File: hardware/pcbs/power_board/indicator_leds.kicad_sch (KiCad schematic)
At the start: 10 parts, among them Q4 BSS138, Q5 BSS138, Q6 BSS138

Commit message: audio_board, power_board: update shop and part links
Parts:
- R35, R36, R37: Part (none) -> R 10Ω 125mW 5% 0805
- R38, R39, R40: Part (none) -> R 1.8kΩ 125mW 5% 0805
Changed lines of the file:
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@@
+			)
+		)
+		(property "Part" "R 10Ω 125mW 5% 0805"
+			(at 123.19 96.52 0)
+			(effects
+				(font
+					(size 1.27 1.27)
+				)
+				(hide yes)
 			)
 		)
@@
 		)
 		(property "LCSC" "C17415"
+			(at 123.19 132.08 0)
+			(effects
+				(font
+					(size 1.27 1.27)
+				)
+				(hide yes)
+			)
+		)
+		(property "Part" "R 10Ω 125mW 5% 0805"
 			(at 123.19 132.08 0)
 			(effects
@@
 			)
 		)
+		(property "Part" "R 1.8kΩ 125mW 5% 0805"
+			(at 153.67 64.77 0)
+			(effects
+				(font
+					(size 1.27 1.27)
+				)
+				(hide yes)
+			)
+		)
 		(pin "2"
 		)
@@
 			)
 		)
+		(property "Part" "R 1.8kΩ 125mW 5% 0805"
+			(at 148.59 64.77 0)
+			(effects
+				(font
+					(size 1.27 1.27)
+				)
+				(hide yes)
+			)
+		)
 		(pin "2"
 		)
@@
 			)
 		)
+		(property "Part" "R 10Ω 125mW 5% 0805"
+			(at 123.19 114.3 0)
+			(effects
+				(font
+					(size 1.27 1.27)
+				)
+				(hide yes)
+			)
+		)
 		(pin "1"
 		)
@@
 			(at 143.51 64.77 0)
 			(effects
+				(font
+					(size 1.27 1.27)
+				)
+				(hide yes)
+			)
+		)
+		(property "Part" "R 1.8kΩ 125mW 5% 0805"
+			(at 143.51 64.77 0)
+			(effects

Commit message: power_board: BIGGER inductors
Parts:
- R35, R36, R37: value 10Ω -> 10Ω
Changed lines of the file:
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@@
 			)
 		)
-		(property "Value" "10Ω "
+		(property "Value" "10Ω"
 			(at 123.19 99.06 90)
 			(effects
@@
 			)
 		)
-		(property "Value" "10Ω "
+		(property "Value" "10Ω"
 			(at 123.19 134.62 90)
 			(effects
@@
 			)
 		)
-		(property "Value" "10Ω "
+		(property "Value" "10Ω"
 			(at 123.19 116.84 90)
 			(effects

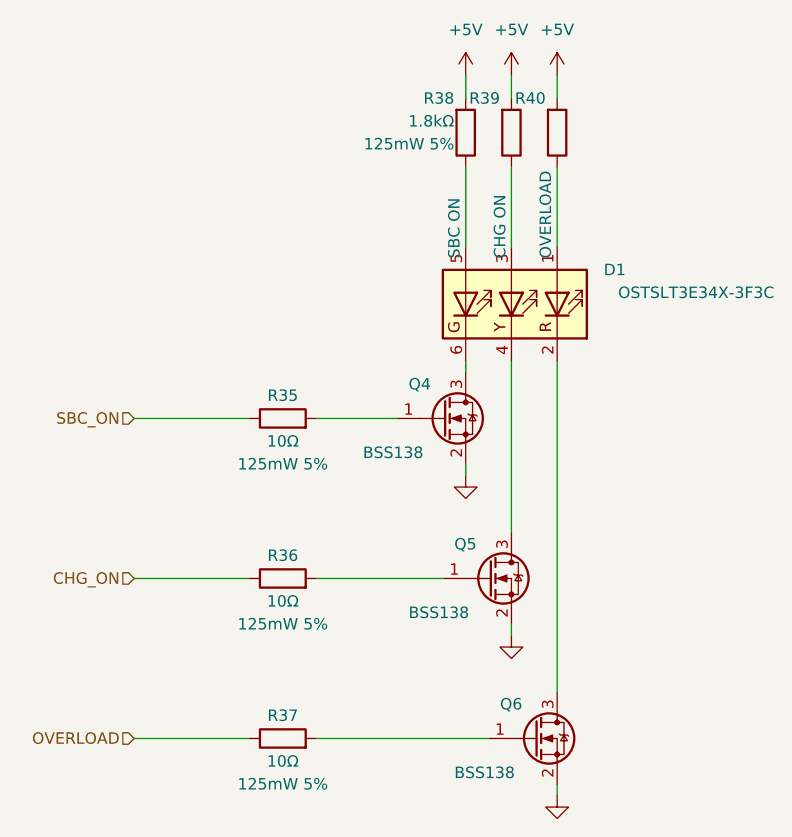
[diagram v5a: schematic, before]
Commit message: power_board: use USB3-A passthrough connector and fix chg EN
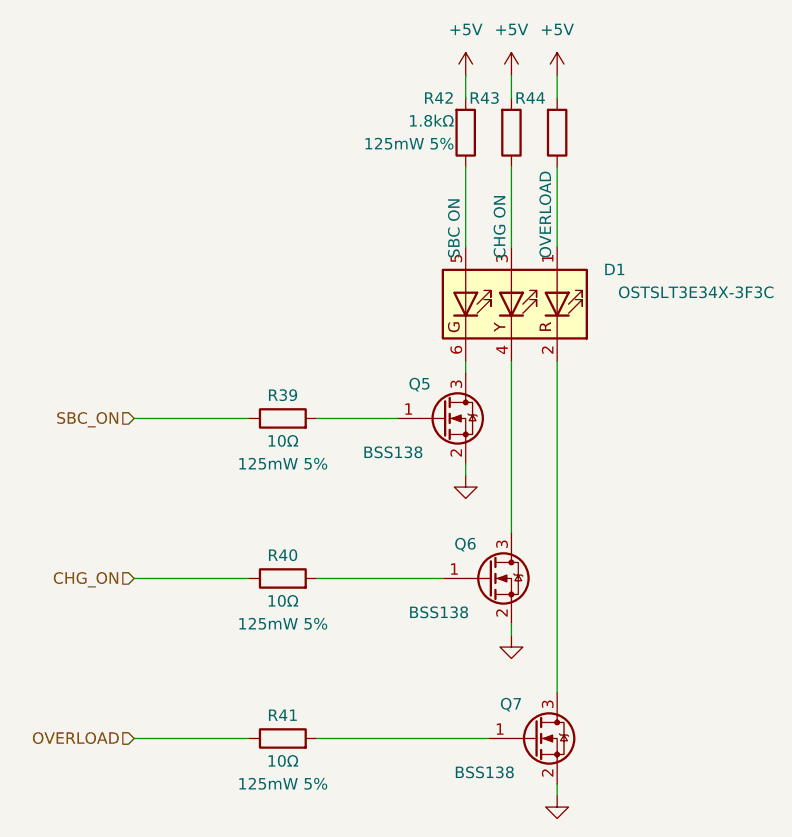
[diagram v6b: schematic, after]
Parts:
- renumbered Q4 to Q5, Q5 to Q6, Q6 to Q7, R35 to R39, R36 to R40, R37 to R41, R38 to R42, R39 to R43, R40 to R44
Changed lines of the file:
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@@
 		(on_board yes)
 		(dnp no)
-		(property "Reference" "Q6"
+		(property "Reference" "Q7"
 			(at 147.32 128.27 0)
 			(effects
@@
 			(project "power_board"
 				(path "/4b166175-80a4-48c6-994d-6e62a6160b87/9db409a6-3616-4139-9d4b-1b510fbe4a7d"
-					(reference "Q6")
+					(reference "Q7")
 					(unit 1)
 				)
@@
 		(on_board yes)
 		(dnp no)
-		(property "Reference" "R35"
+		(property "Reference" "R39"
 			(at 123.19 93.98 90)
 			(effects
@@
 			(project "power_board"
 				(path "/4b166175-80a4-48c6-994d-6e62a6160b87/9db409a6-3616-4139-9d4b-1b510fbe4a7d"
-					(reference "R35")
+					(reference "R39")
 					(unit 1)
 				)
@@
 		(on_board yes)
 		(dnp no)
-		(property "Reference" "R37"
+		(property "Reference" "R41"
 			(at 123.19 129.54 90)
 			(effects
@@
 			(project "power_board"
 				(path "/4b166175-80a4-48c6-994d-6e62a6160b87/9db409a6-3616-4139-9d4b-1b510fbe4a7d"
-					(reference "R37")
+					(reference "R41")
 					(unit 1)
 				)
@@
 		(on_board yes)
 		(dnp no)
-		(property "Reference" "R40"
+		(property "Reference" "R44"
 			(at 152.4 60.96 0)
 			(effects
@@
 			(project "power_board"
 				(path "/4b166175-80a4-48c6-994d-6e62a6160b87/9db409a6-3616-4139-9d4b-1b510fbe4a7d"
-					(reference "R40")
+					(reference "R44")
 					(unit 1)
 				)
@@
 		(on_board yes)
 		(dnp no)
-		(property "Reference" "R39"
+		(property "Reference" "R43"
 			(at 147.32 60.96 0)
 			(effects
@@
 			(project "power_board"
 				(path "/4b166175-80a4-48c6-994d-6e62a6160b87/9db409a6-3616-4139-9d4b-1b510fbe4a7d"
-					(reference "R39")
+					(reference "R43")
 					(unit 1)
 				)
@@
 		(on_board yes)
 		(dnp no)
-		(property "Reference" "R36"
+		(property "Reference" "R40"
 			(at 123.19 111.76 90)
 			(effects
@@
 			(project "power_board"
 				(path "/4b166175-80a4-48c6-994d-6e62a6160b87/9db409a6-3616-4139-9d4b-1b510fbe4a7d"
-					(reference "R36")
+					(reference "R40")
 					(unit 1)
 				)
@@
 		(on_board yes)
 		(dnp no)
-		(property "Reference" "Q4"
+		(property "Reference" "Q5"
 			(at 137.16 92.71 0)
 			(effects
@@
 			(project "power_board"
 				(path "/4b166175-80a4-48c6-994d-6e62a6160b87/9db409a6-3616-4139-9d4b-1b510fbe4a7d"
-					(reference "Q4")
+					(reference "Q5")
 					(unit 1)
 				)
@@
 		(on_board yes)
 		(dnp no)
-		(property "Reference" "R38"
+		(property "Reference" "R42"
 			(at 142.24 60.96 0)
 			(effects
@@
 			(project "power_board"
 				(path "/4b166175-80a4-48c6-994d-6e62a6160b87/9db409a6-3616-4139-9d4b-1b510fbe4a7d"
-					(reference "R38")
+					(reference "R42")
 					(unit 1)
 				)
@@
 		(on_board yes)
 		(dnp no)
-		(property "Reference" "Q5"
+		(property "Reference" "Q6"
 			(at 142.24 110.49 0)
 			(effects
@@
 			(project "power_board"
 				(path "/4b166175-80a4-48c6-994d-6e62a6160b87/9db409a6-3616-4139-9d4b-1b510fbe4a7d"
-					(reference "Q5")
-					(unit 1)
-				)
+					(reference "Q6")
+					(unit 1)
+				)

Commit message: power_board: add protection resistor to overload signal
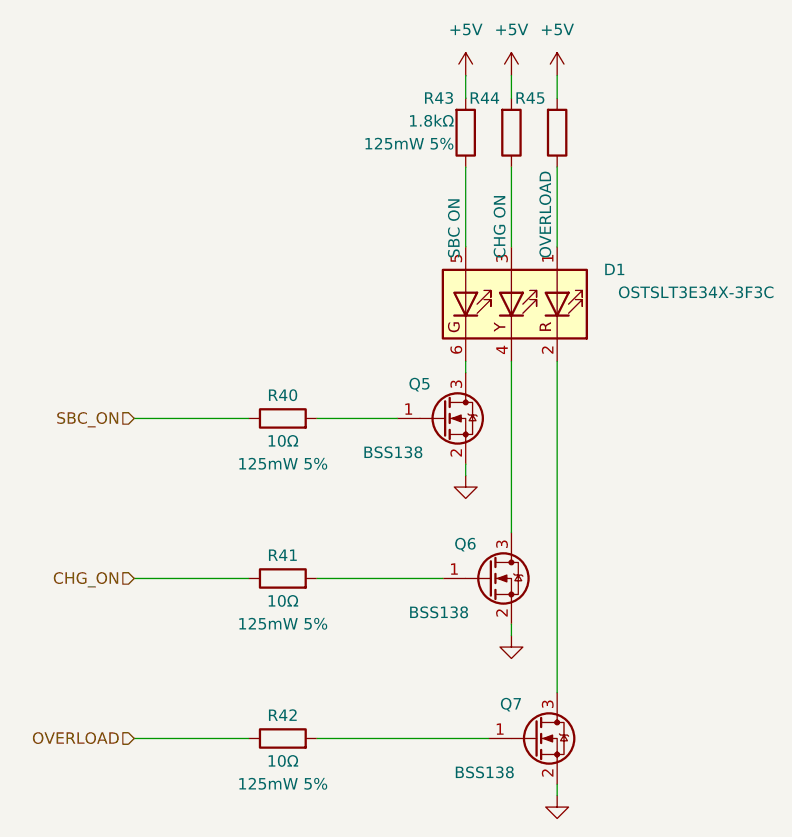
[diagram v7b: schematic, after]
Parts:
- renumbered R39 to R40, R40 to R41, R41 to R42, R42 to R43, R43 to R44, R44 to R45
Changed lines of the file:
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@@
 		(on_board yes)
 		(dnp no)
-		(property "Reference" "R39"
+		(property "Reference" "R40"
 			(at 123.19 93.98 90)
 			(effects
@@
 			(project "power_board"
 				(path "/4b166175-80a4-48c6-994d-6e62a6160b87/9db409a6-3616-4139-9d4b-1b510fbe4a7d"
-					(reference "R39")
+					(reference "R40")
 					(unit 1)
 				)
@@
 		(on_board yes)
 		(dnp no)
-		(property "Reference" "R41"
+		(property "Reference" "R42"
 			(at 123.19 129.54 90)
 			(effects
@@
 			(project "power_board"
 				(path "/4b166175-80a4-48c6-994d-6e62a6160b87/9db409a6-3616-4139-9d4b-1b510fbe4a7d"
-					(reference "R41")
+					(reference "R42")
 					(unit 1)
 				)
@@
 		(on_board yes)
 		(dnp no)
-		(property "Reference" "R44"
+		(property "Reference" "R45"
 			(at 152.4 60.96 0)
 			(effects
@@
 			(project "power_board"
 				(path "/4b166175-80a4-48c6-994d-6e62a6160b87/9db409a6-3616-4139-9d4b-1b510fbe4a7d"
-					(reference "R44")
+					(reference "R45")
 					(unit 1)
 				)
@@
 		(on_board yes)
 		(dnp no)
-		(property "Reference" "R43"
+		(property "Reference" "R44"
 			(at 147.32 60.96 0)
 			(effects
@@
 			(project "power_board"
 				(path "/4b166175-80a4-48c6-994d-6e62a6160b87/9db409a6-3616-4139-9d4b-1b510fbe4a7d"
-					(reference "R43")
+					(reference "R44")
 					(unit 1)
 				)
@@
 		(on_board yes)
 		(dnp no)
-		(property "Reference" "R40"
+		(property "Reference" "R41"
 			(at 123.19 111.76 90)
 			(effects
@@
 			(project "power_board"
 				(path "/4b166175-80a4-48c6-994d-6e62a6160b87/9db409a6-3616-4139-9d4b-1b510fbe4a7d"
-					(reference "R40")
+					(reference "R41")
 					(unit 1)
 				)
@@
 		(on_board yes)
 		(dnp no)
-		(property "Reference" "R42"
+		(property "Reference" "R43"
 			(at 142.24 60.96 0)
 			(effects
@@
 			(project "power_board"
 				(path "/4b166175-80a4-48c6-994d-6e62a6160b87/9db409a6-3616-4139-9d4b-1b510fbe4a7d"
-					(reference "R42")
-					(unit 1)
-				)
+					(reference "R43")
+					(unit 1)
+				)

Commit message: power_board: proper enable circuit for meanwell power modules
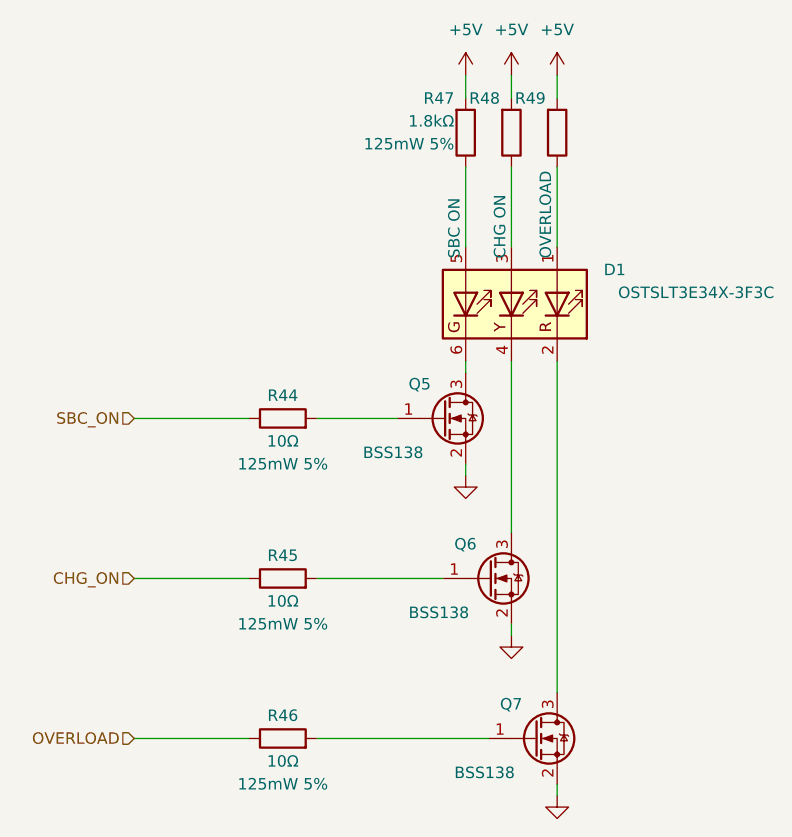
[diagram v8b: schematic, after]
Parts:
- renumbered R40 to R44, R41 to R45, R42 to R46, R43 to R47, R44 to R48, R45 to R49
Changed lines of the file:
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@@
 		(on_board yes)
 		(dnp no)
-		(property "Reference" "R40"
+		(property "Reference" "R44"
 			(at 123.19 93.98 90)
 			(effects
@@
 			(project "power_board"
 				(path "/4b166175-80a4-48c6-994d-6e62a6160b87/9db409a6-3616-4139-9d4b-1b510fbe4a7d"
-					(reference "R40")
+					(reference "R44")
 					(unit 1)
 				)
@@
 		(on_board yes)
 		(dnp no)
-		(property "Reference" "R42"
+		(property "Reference" "R46"
 			(at 123.19 129.54 90)
 			(effects
@@
 			(project "power_board"
 				(path "/4b166175-80a4-48c6-994d-6e62a6160b87/9db409a6-3616-4139-9d4b-1b510fbe4a7d"
-					(reference "R42")
+					(reference "R46")
 					(unit 1)
 				)
@@
 		(on_board yes)
 		(dnp no)
-		(property "Reference" "R45"
+		(property "Reference" "R49"
 			(at 152.4 60.96 0)
 			(effects
@@
 			(project "power_board"
 				(path "/4b166175-80a4-48c6-994d-6e62a6160b87/9db409a6-3616-4139-9d4b-1b510fbe4a7d"
-					(reference "R45")
+					(reference "R49")
 					(unit 1)
 				)
@@
 		(on_board yes)
 		(dnp no)
-		(property "Reference" "R44"
+		(property "Reference" "R48"
 			(at 147.32 60.96 0)
 			(effects
@@
 			(project "power_board"
 				(path "/4b166175-80a4-48c6-994d-6e62a6160b87/9db409a6-3616-4139-9d4b-1b510fbe4a7d"
-					(reference "R44")
+					(reference "R48")
 					(unit 1)
 				)
@@
 		(on_board yes)
 		(dnp no)
-		(property "Reference" "R41"
+		(property "Reference" "R45"
 			(at 123.19 111.76 90)
 			(effects
@@
 			(project "power_board"
 				(path "/4b166175-80a4-48c6-994d-6e62a6160b87/9db409a6-3616-4139-9d4b-1b510fbe4a7d"
-					(reference "R41")
+					(reference "R45")
 					(unit 1)
 				)
@@
 		(on_board yes)
 		(dnp no)
-		(property "Reference" "R43"
+		(property "Reference" "R47"
 			(at 142.24 60.96 0)
 			(effects
@@
 			(project "power_board"
 				(path "/4b166175-80a4-48c6-994d-6e62a6160b87/9db409a6-3616-4139-9d4b-1b510fbe4a7d"
-					(reference "R43")
-					(unit 1)
-				)
+					(reference "R47")
+					(unit 1)
+				)
